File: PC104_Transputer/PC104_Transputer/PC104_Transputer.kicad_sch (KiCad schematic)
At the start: 28 parts, among them J3 Conn_02x08_Odd_Even, J5 Conn_02x05_Odd_Even, U1 ATF1502AS-xAx44, U11 IMSC011, U2 74LS244_Split, U4 74HC245, U8 TRAM, Y1 CXO_DIP8

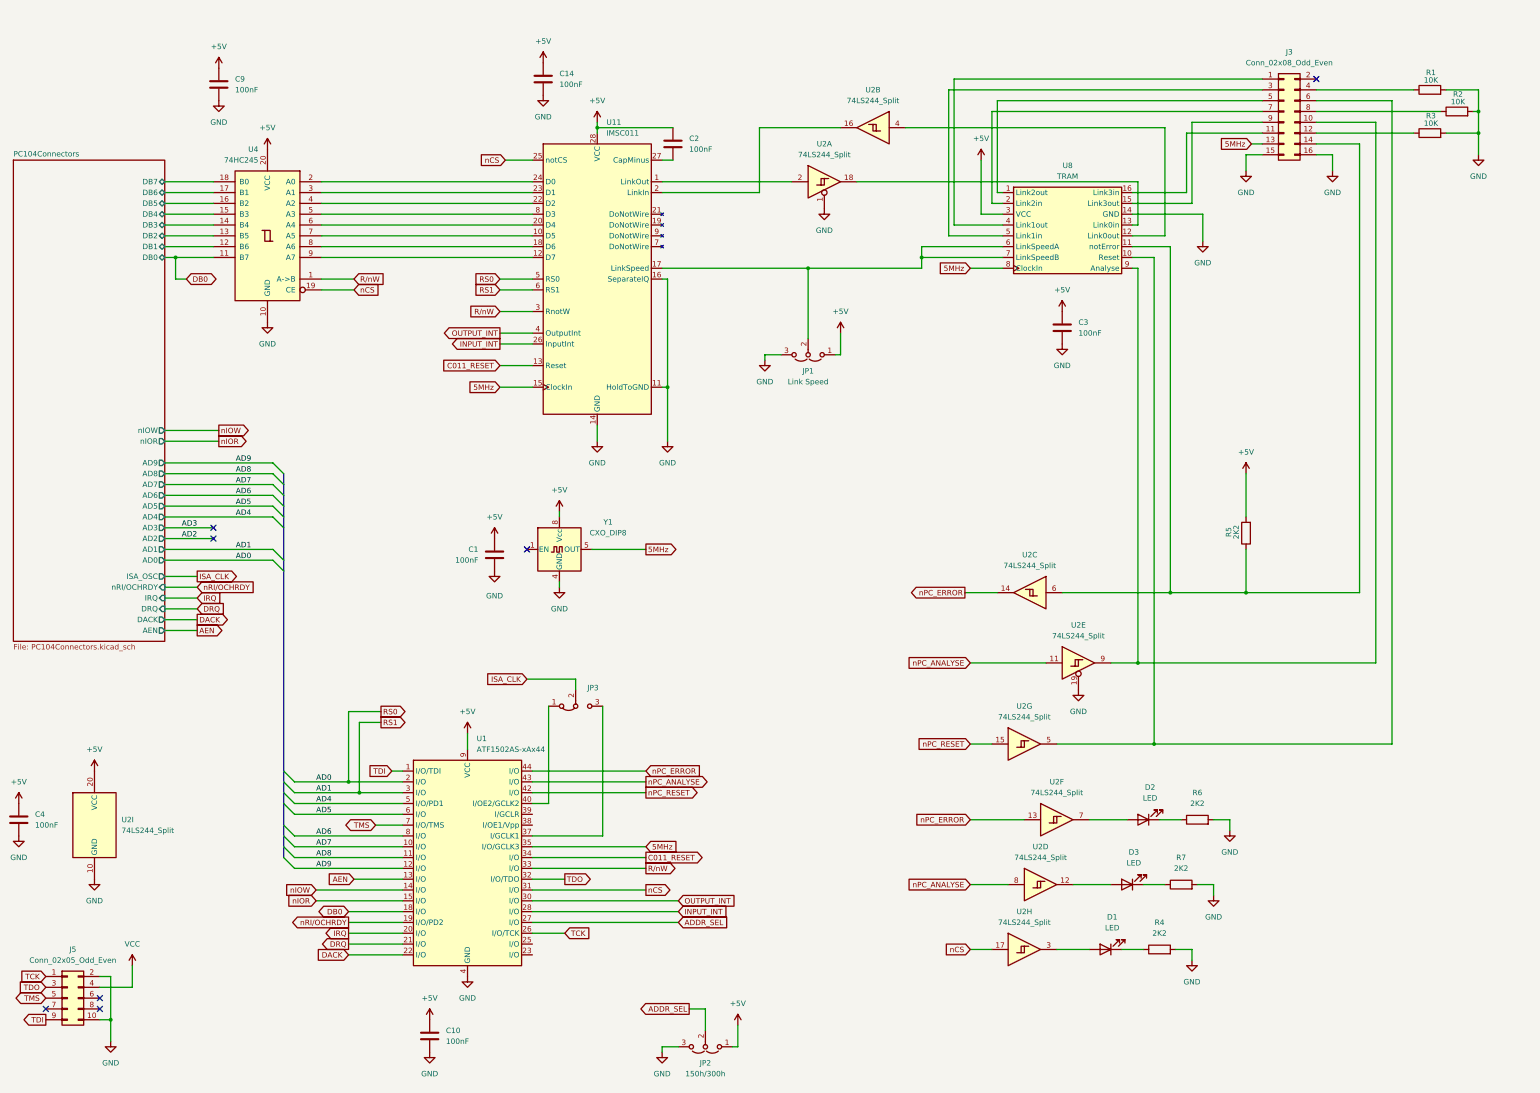
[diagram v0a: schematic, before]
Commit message: Fixing a few things
Fixed a couple of minor things with the schematic and board for both cards
Also created Schematics
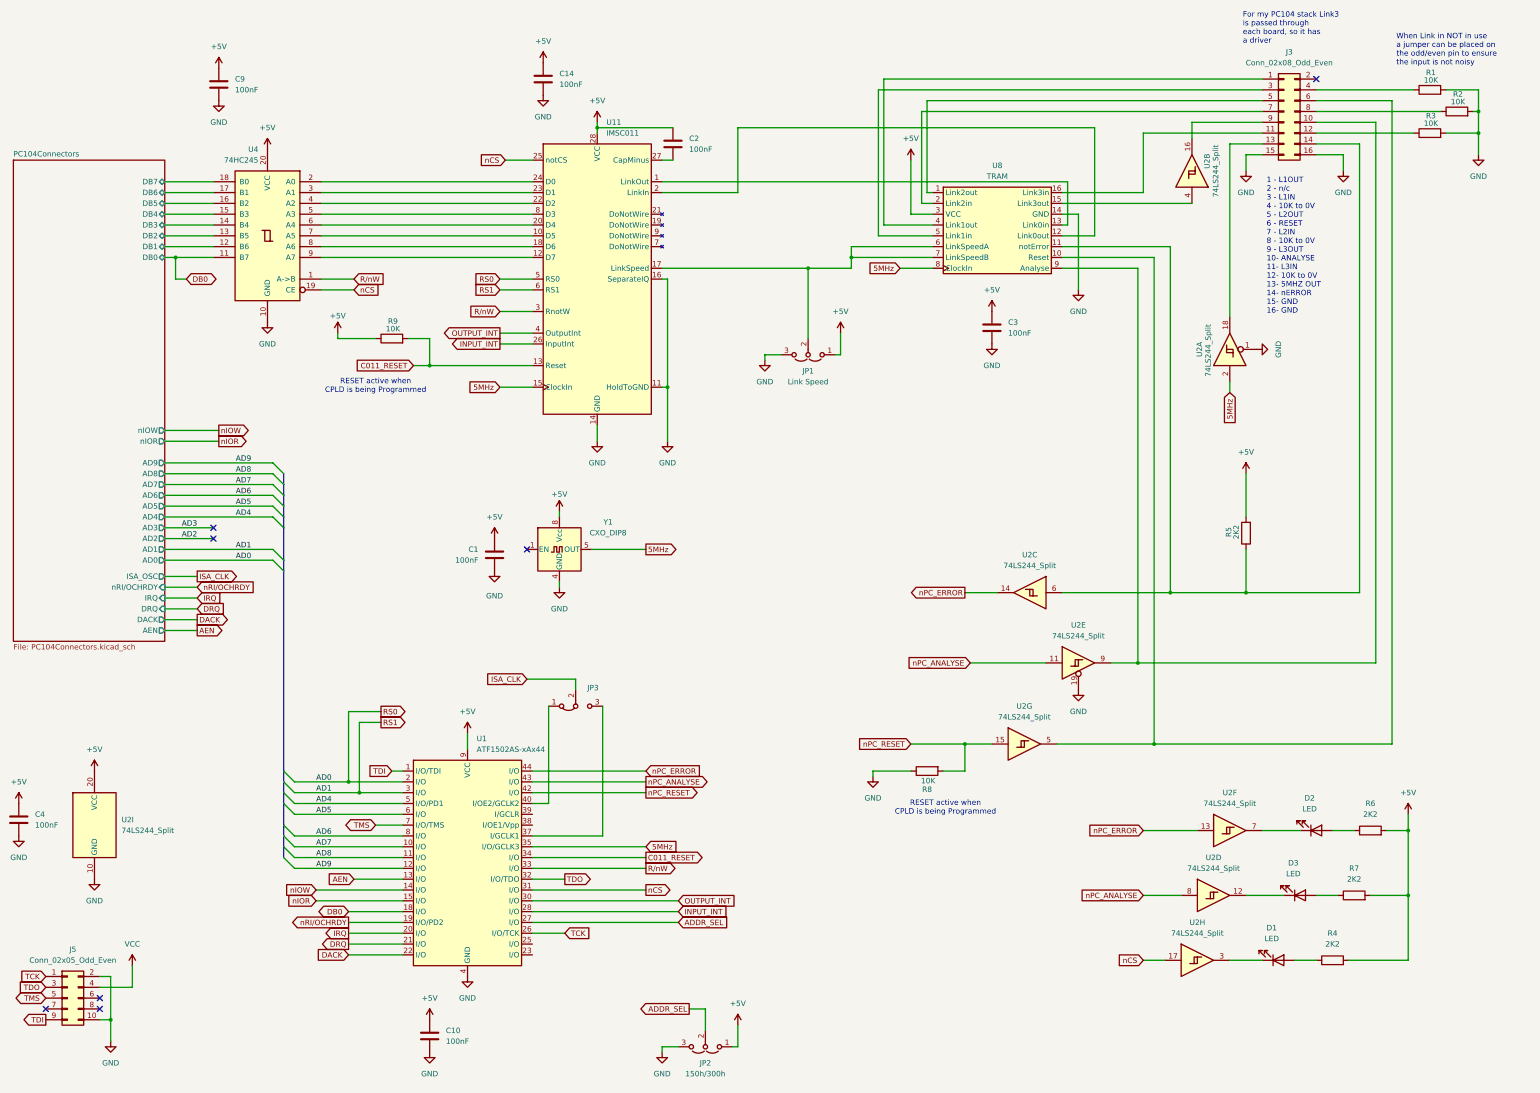
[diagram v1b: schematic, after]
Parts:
- added R8, R9: 10K, Resistor_SMD:R_0402_1005Metric, symbol Device:R
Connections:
- net +5V: now also R4.2, R6.2, R7.2, R9.1
- net 5MHz: now also U2.2; no longer J3.13 (Pin_13)
- net C011_RESET: now also R9.2
- net GND: now also R8.1; no longer R4.2, R6.2, R7.2
- net nPC_RESET: now also R8.2
- net at R7.1: now also D3.2 (A); no longer D3.1 (K)
- net at U2.12: now also D3.1 (K); no longer D3.2 (A)
- net at U2.7: now also D2.1 (K); no longer D2.2 (A)
- net at U11.1 (LinkOut): now also U8.13 (Link0in); no longer U2.2
- net at U11.2 (LinkIn): now also U8.12 (Link0out); no longer U2.16
- net at U2.3: now also D1.1 (K); no longer D1.2 (A)
- net at U2.4: now also U8.15 (Link3out); no longer U8.12 (Link0out)
- net at U2.18: now also J3.13 (Pin_13); no longer U8.13 (Link0in)
- net at J3.9 (Pin_9): now also U2.16; no longer U8.15 (Link3out)
- net at R4.1: now also D1.2 (A); no longer D1.1 (K)
- net at R6.1: now also D2.2 (A); no longer D2.1 (K)
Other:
- note added: "1 - L1OUT 2 - n/c 3 - L1IN 4 - 10K to 0V 5 - L2OUT 6 - RESET 7 - L2IN 8 - 10K to 0V 9 - L3OUT 10- ANALYSE 11- L3IN 12- 10K to 0V 13- 5MHZ OUT 14- nERROR 15- GND 16- GND"
- note added: "For my PC104 stack Link3 is passed through each board, so it has a driver"
- note added: "RESET active when CPLD is being Programmed"
- note added: "When Link in NOT in use a jumper can be placed on the odd/even pin to ensure the input is not noisy"
- moved on the sheet: C3, D1, D2, D3, R4, R6, R7, U2A, U2B, U2D, U2F, U2H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

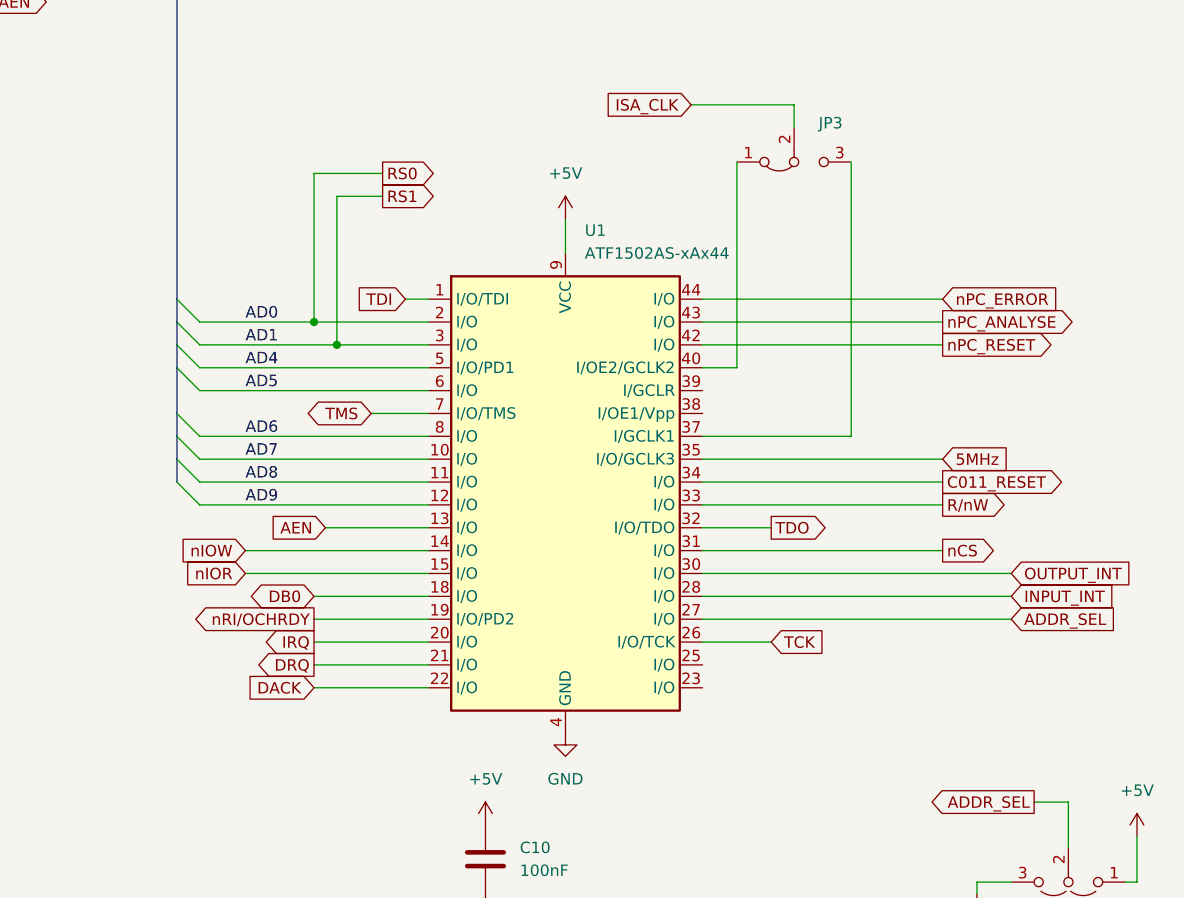
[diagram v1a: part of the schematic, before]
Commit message: Fixed CPLD pinout
Fixed the CPLD pin out which would never have worked with the previous version due to the PLCC and TQFP pinouts being different
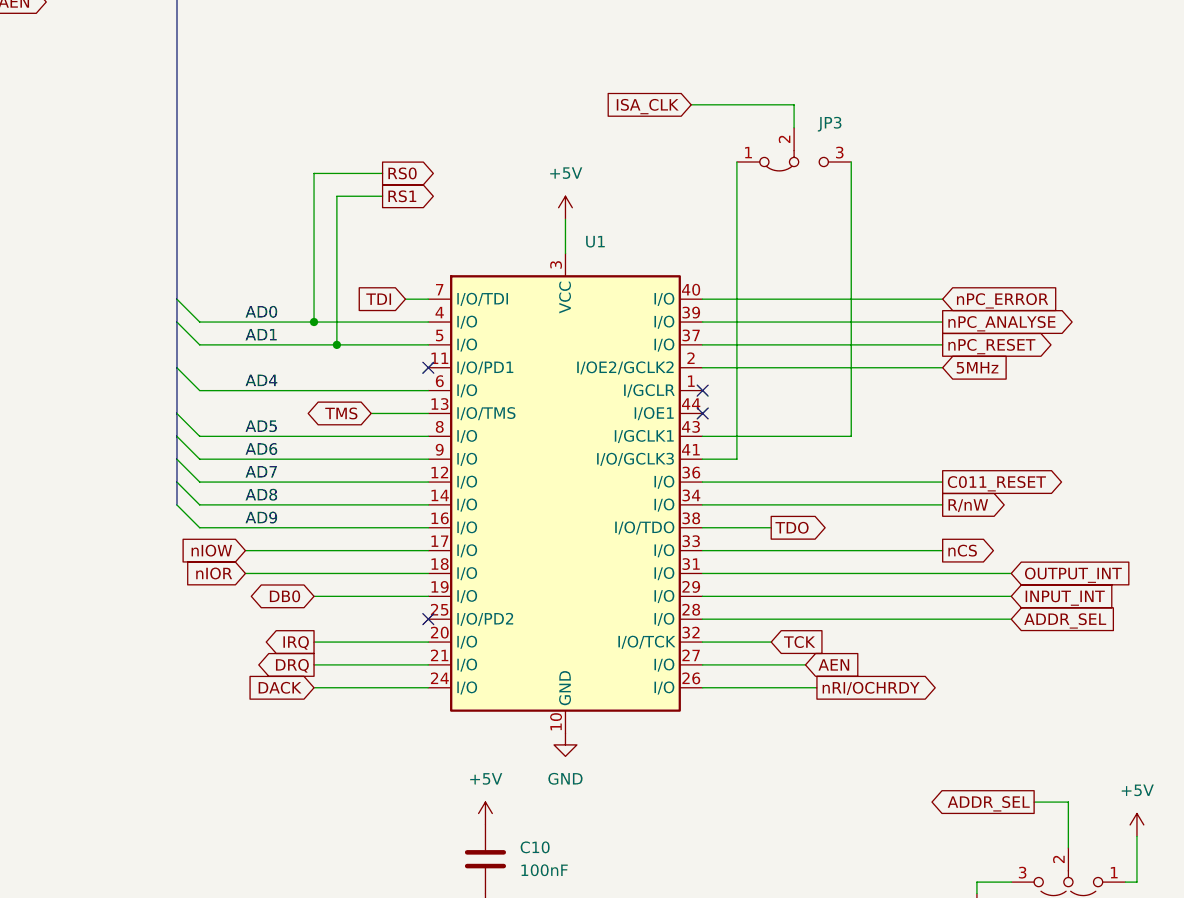
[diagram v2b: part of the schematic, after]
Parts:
- removed U1: ATF1502AS-xAx44, Package_LCC:PLCC-44_THT-Socket, symbol CPLD_Microchip:ATF1502AS-xAx44
- added U1: ~, Package_LCC:PLCC-44_THT-Socket, symbol PaulasKiCAD:ATF1502AS_PLCC
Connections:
- net +5V: now also U1.15 (VCC), U1.23 (VCC), U1.3 (VCC), U1.35 (VCC)
- net 5MHz: now also U1.2 (I/OE2/GCLK2)
- net AD4: now also U1.6 (I/O)
- net AD5: now also U1.8 (I/O)
- net AD6: now also U1.9 (I/O)
- net AD7: now also U1.12 (I/O)
- net AD8: now also U1.14 (I/O)
- net AD9: now also U1.16 (I/O)
- net ADDR_SEL: now also U1.28 (I/O)
- net AEN: now also U1.27 (I/O)
- net C011_RESET: now also U1.36 (I/O)
- net DACK: now also U1.24 (I/O)
- net DB0: now also U1.19 (I/O)
- net DRQ: now also U1.21 (I/O)
- net GND: now also U1.10 (GND), U1.22 (GND), U1.30 (GND), U1.42 (GND)
- net INPUT_INT: now also U1.29 (I/O)
- net IRQ: now also U1.20 (I/O)
- net OUTPUT_INT: now also U1.31 (I/O)
- net RS0: now also U1.4 (I/O)
- net RS1: now also U1.5 (I/O)
- net R/nW: now also U1.34 (I/O)
- net TCK: now also U1.32 (I/O/TCK)
- net TDI: now also U1.7 (I/O/TDI)
- net TDO: now also U1.38 (I/O/TDO)
- net TMS: now also U1.13 (I/O/TMS)
- net nCS: now also U1.33 (I/O)
- net nIOR: now also U1.18 (I/O)
- net nIOW: now also U1.17 (I/O)
- net nPC_ANALYSE: now also U1.39 (I/O)
- net nPC_ERROR: now also U1.40 (I/O)
- net nPC_RESET: now also U1.37 (I/O)
- net nRI/OCHRDY: now also U1.26 (I/O)
- net at JP3.3 (B): now also U1.43 (I/GCLK1)
- net at JP3.1 (A): now also U1.41 (I/O/GCLK3)
- no-connect marks 7 -> 11

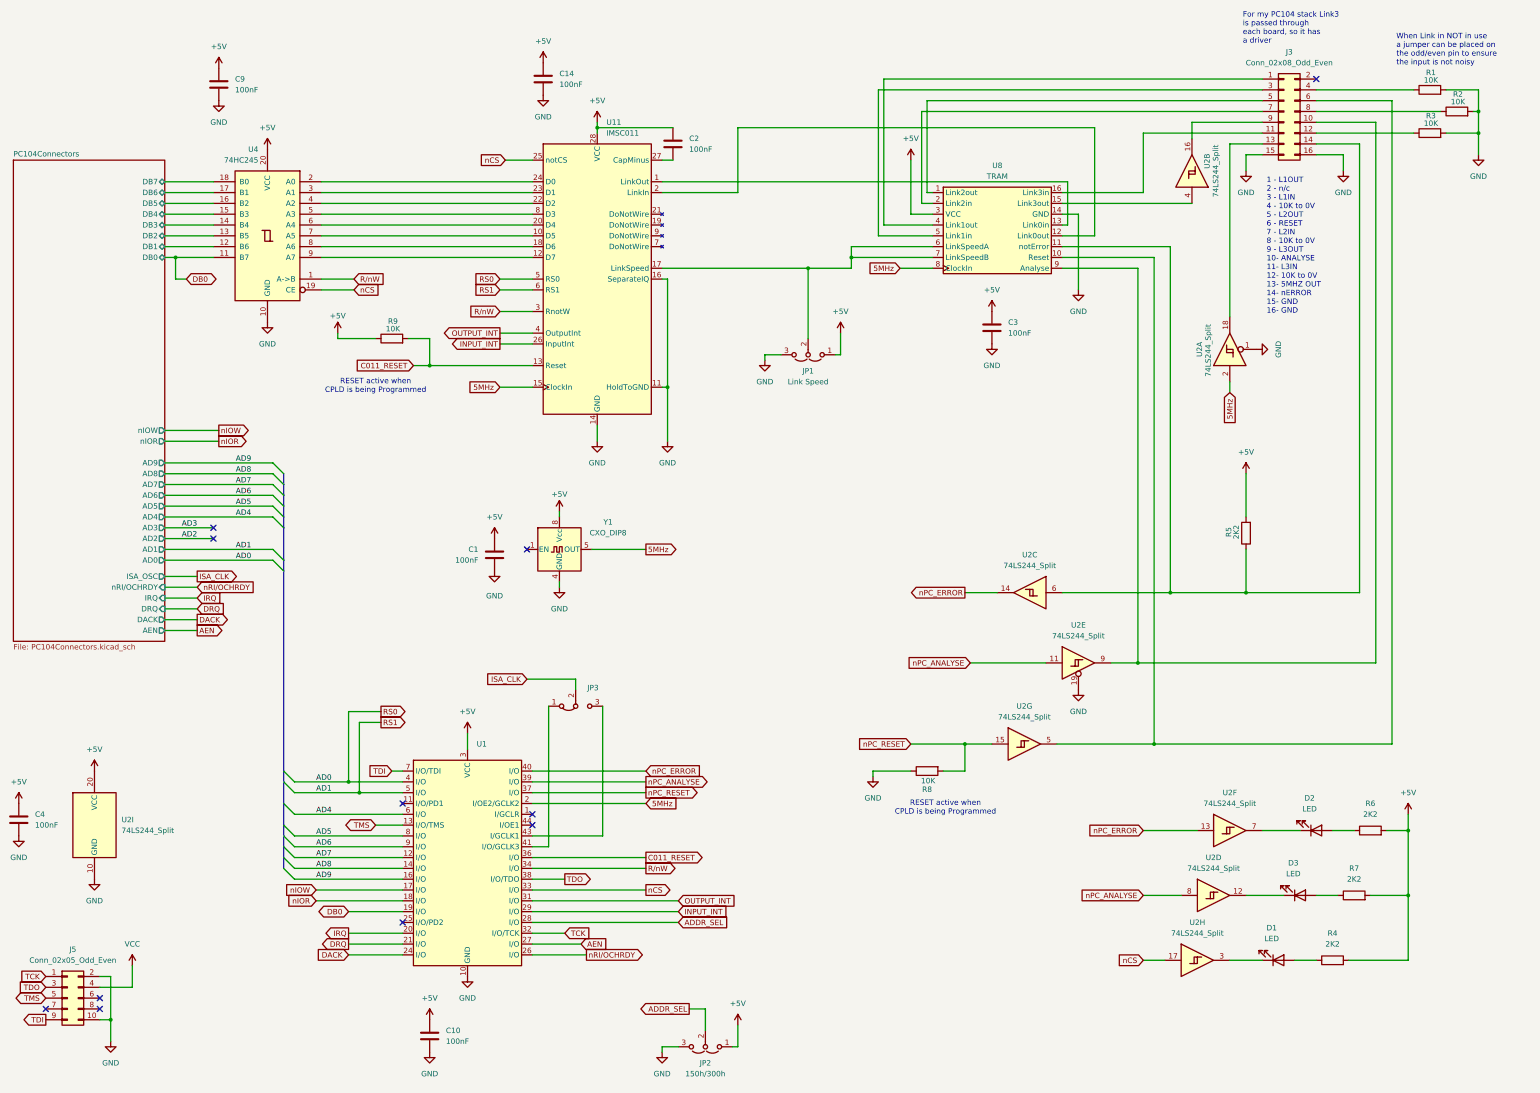
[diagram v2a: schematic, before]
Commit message: Fixed error with PCB, added CPLD files
CPLD files tested on breadboard with a bunch of wires. PCB mistake fixed.
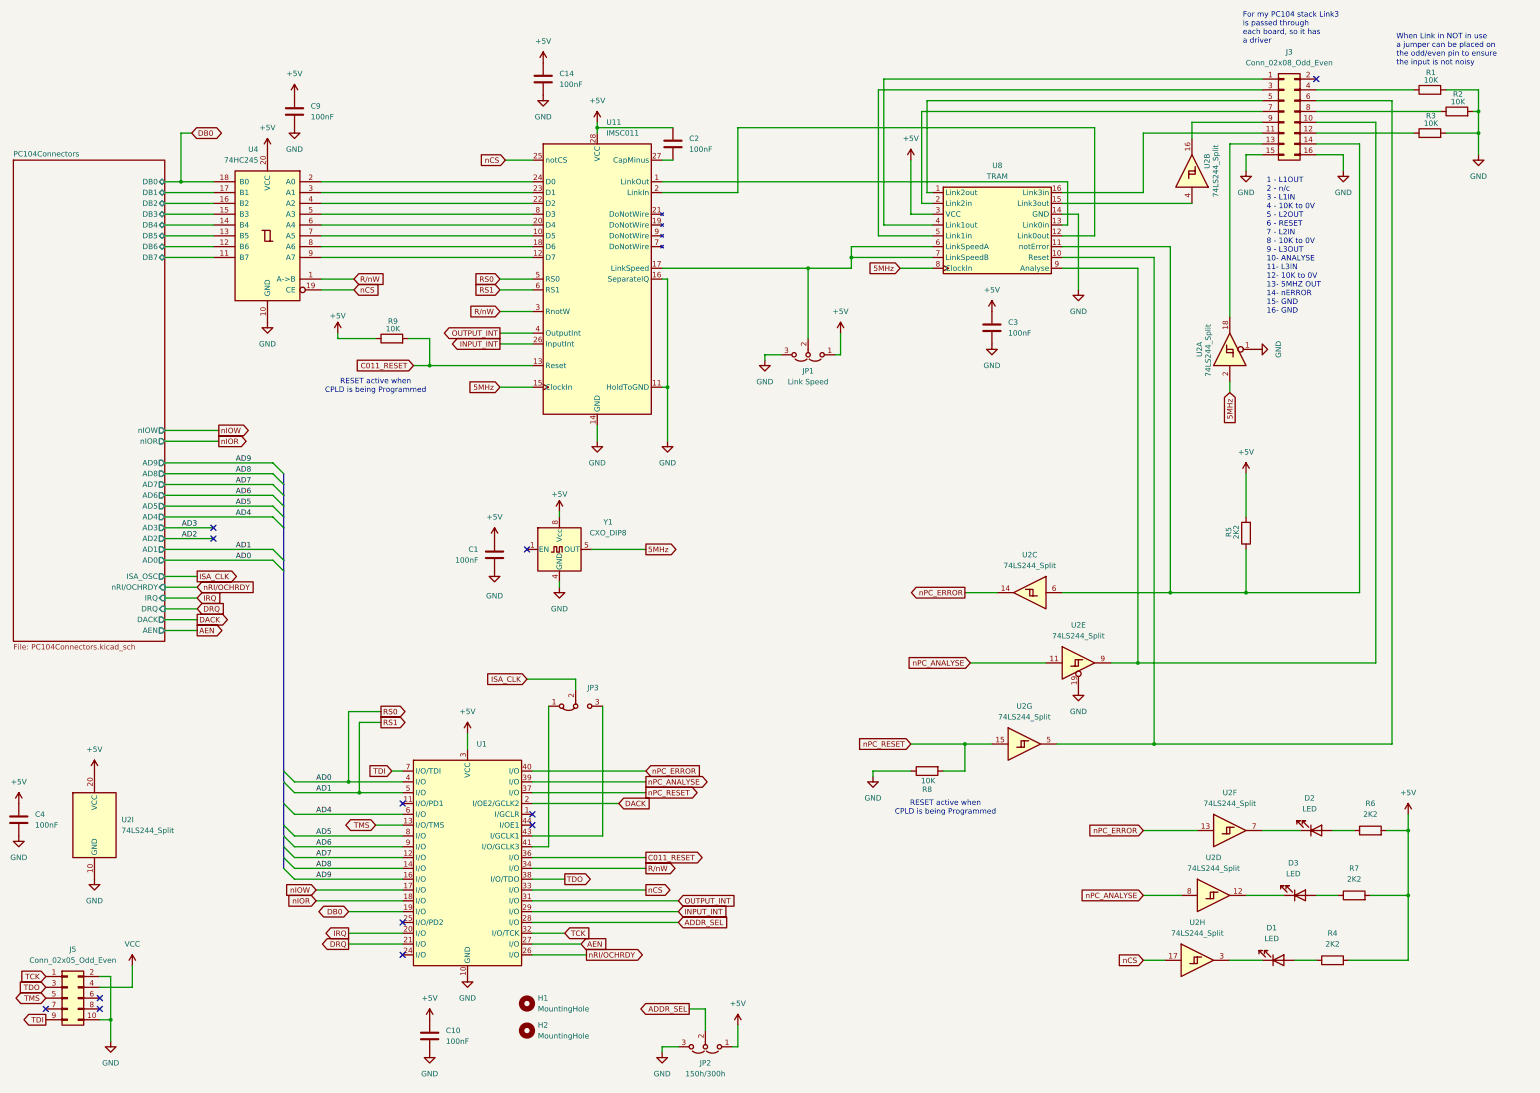
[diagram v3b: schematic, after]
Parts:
- added H1, H2: MountingHole, MountingHole:MountingHole_2.5mm, symbol Mechanical:MountingHole
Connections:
- net 5MHz: no longer U1.2 (I/OE2/GCLK2)
- net DACK: now also U1.2 (I/OE2/GCLK2); no longer U1.24 (I/O)
- net DB0: now also U4.18 (B0); no longer U4.11 (B7)
- net PC104Connectors/DB1: now also U4.17 (B1); no longer U4.12 (B6)
- net PC104Connectors/DB2: now also U4.16 (B2); no longer U4.13 (B5)
- net PC104Connectors/DB3: now also U4.15 (B3); no longer U4.14 (B4)
- net PC104Connectors/DB4: now also U4.14 (B4); no longer U4.15 (B3)
- net PC104Connectors/DB5: now also U4.13 (B5); no longer U4.16 (B2)
- net PC104Connectors/DB6: now also U4.12 (B6); no longer U4.17 (B1)
- net PC104Connectors/DB7: now also U4.11 (B7); no longer U4.18 (B0)
- no-connect marks 11 -> 12
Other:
- moved on the sheet: C9
